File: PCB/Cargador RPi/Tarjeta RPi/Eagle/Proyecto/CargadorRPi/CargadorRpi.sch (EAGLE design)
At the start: 10 parts, among them IC1 MCP3208, X1 RASPI_GPIO_B+_PIN

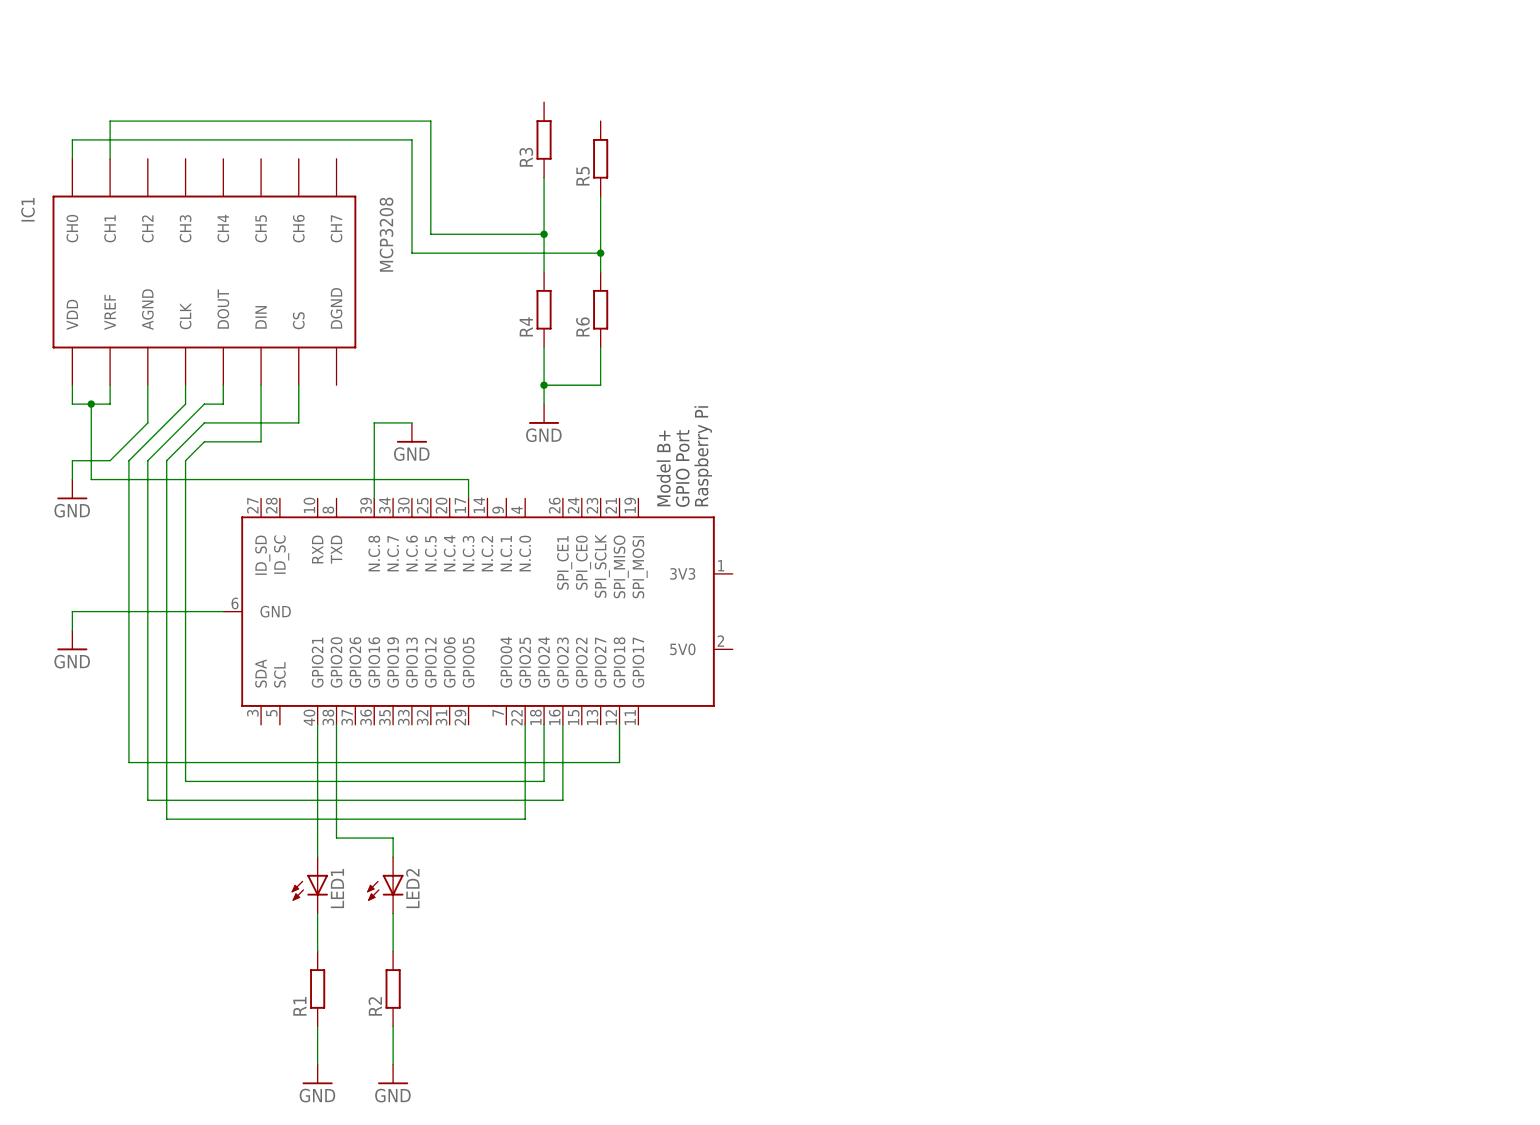
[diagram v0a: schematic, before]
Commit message: Se actualiza el diagrama esquemático del cargador RPi.
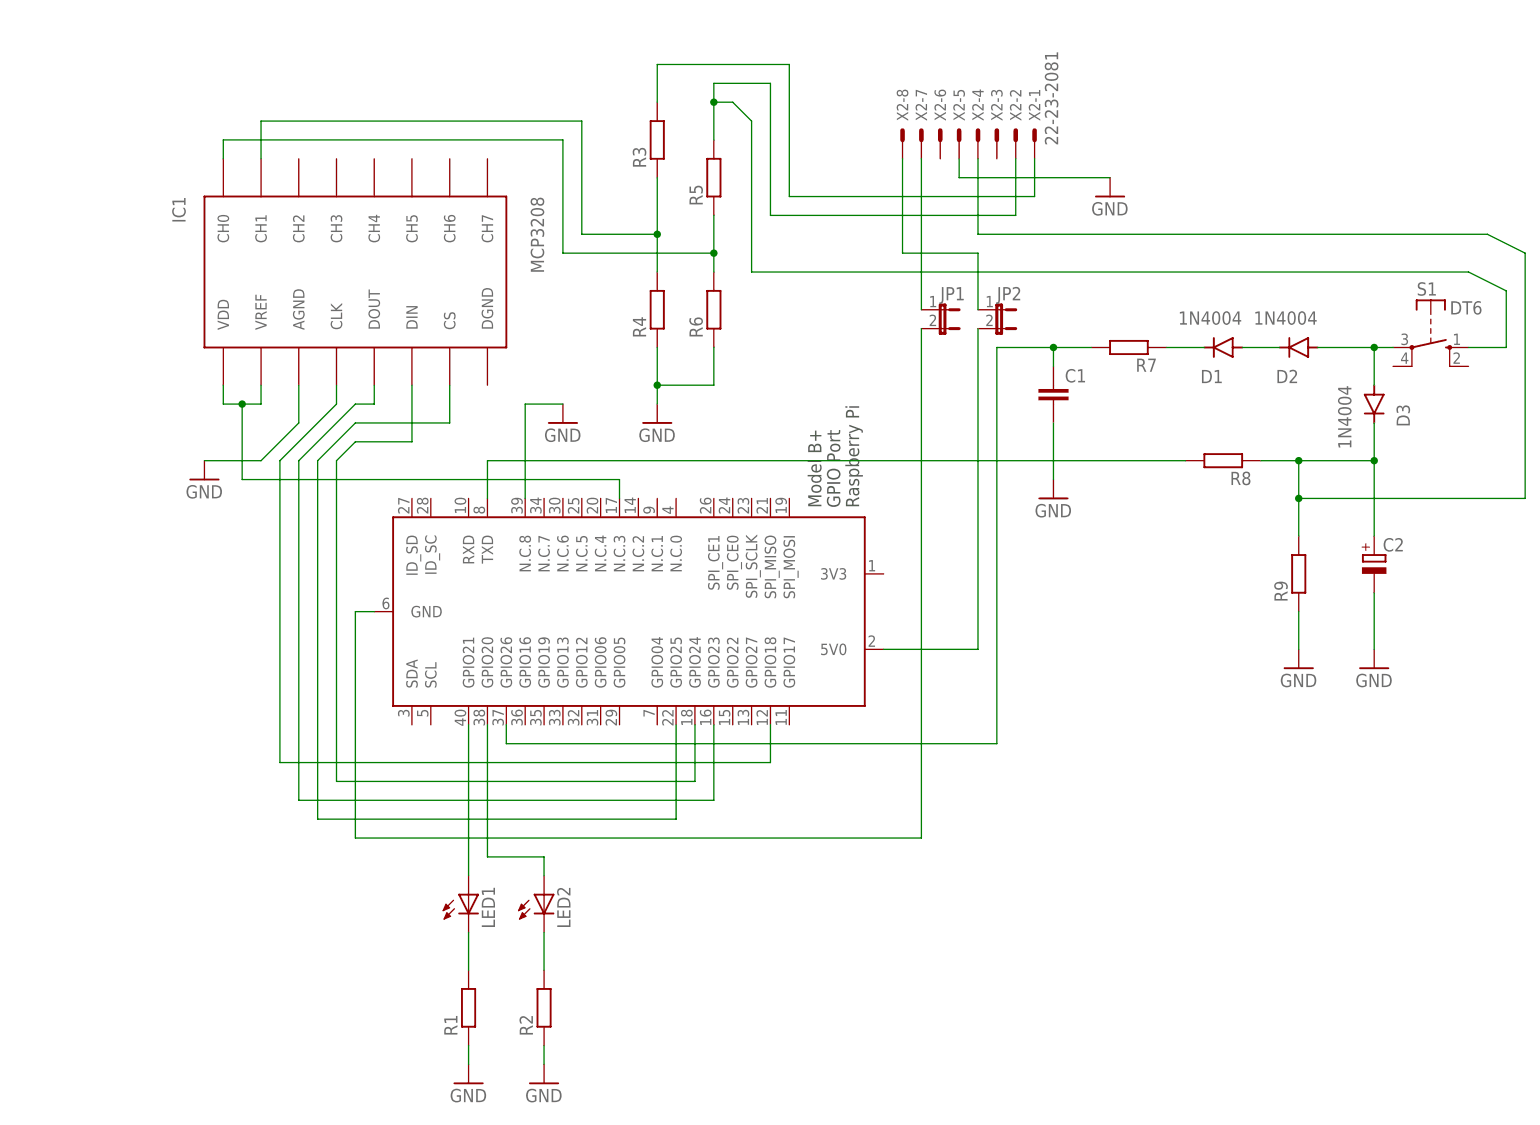
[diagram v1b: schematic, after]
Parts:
- added C1: (no value), capacitor-wima:C2.5/2
- added C2: (no value), rcl:CPOL-EUE5-4
- added D1, D2, D3: 1N4004, diode:1N4004
- added JP1, JP2: (no value), jumper:JP1E
- added R7, R8, R9: (no value), eagle-ltspice:R
- added S1: DT6, switch-misc:DT6
- added X2: 22-23-2081, con-molex:22-23-2081
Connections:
- new net N$12: R3.2, X2-1.S
- new net N$13: R5.2, S1.S, X2-2.S
- new net N$14: JP1.1, X2-7.S
- new net N$15: JP1.2, X1.GND
- new net N$16: JP2.1, X2-8.S
- new net N$17: JP2.2, X1.5V0
- new net N$18: C1.1, R7.2, X1.GPIO26
- new net N$19: D1.C, R7.1
- new net N$20: D1.A, D2.C
- new net N$21: D2.A, D3.A, S1.P
- new net N$22: C2.+, D3.C, R8.1, R9.2, X2-4.S
- new net N$24: R8.2, X1.TXD
- net GND: now also C1.2, C2.-, R9.1, X2-5.S; no longer X1.GND
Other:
- moved on the sheet: IC1, LED1, LED2, R1, R2, R3, R4, R5, R6
